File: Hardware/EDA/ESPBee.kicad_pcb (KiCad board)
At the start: 2 copper layers, 24.4 x 27.6 mm, 8 parts, among them P1 HEADER_M_XBEE_P1-P10_PTH_DTE, P2 HEADER_M_XBEE_P11-P20_PTH_DTE, U1 ESP-12E

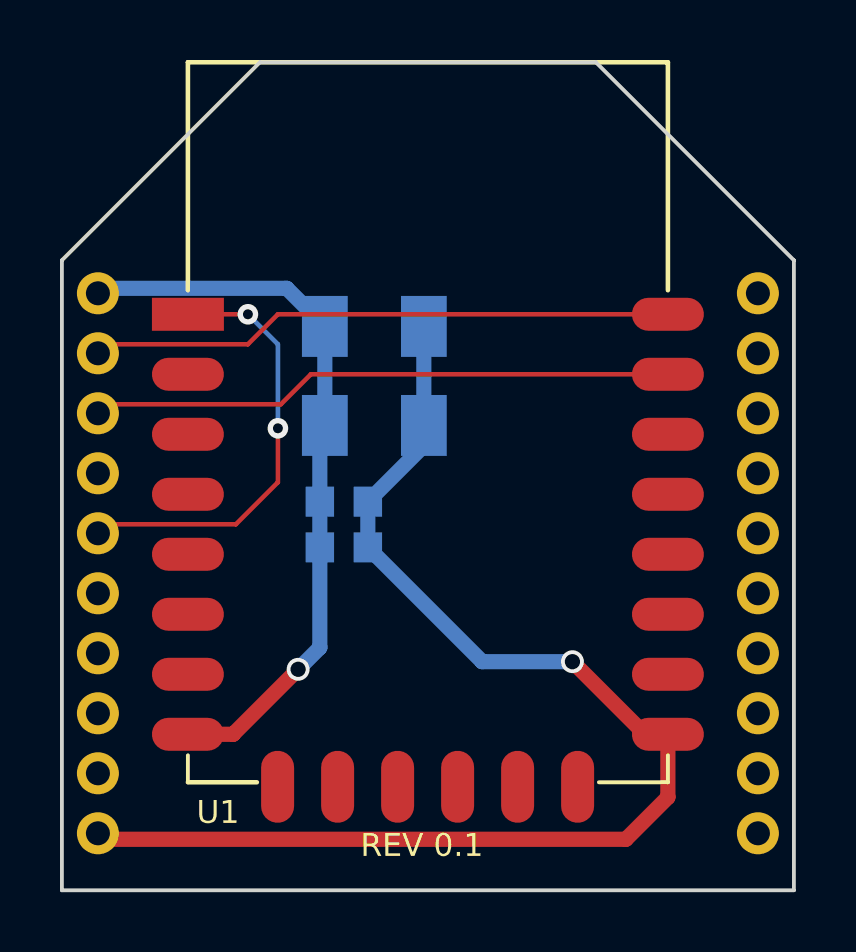
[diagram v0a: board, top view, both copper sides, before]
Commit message: Fixed connections and added pull-up/down resistors for configuration pins.
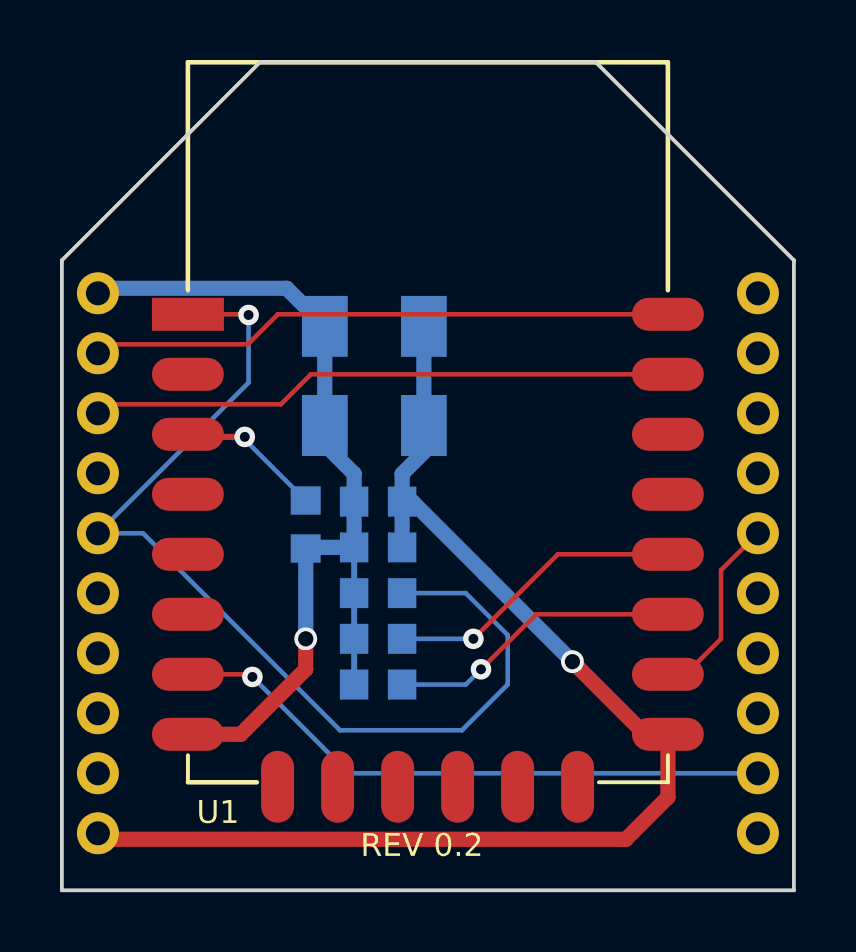
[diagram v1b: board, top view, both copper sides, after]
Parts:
- added R1: 10K, Passive:R0603, B.Cu at (109.5, 95.1)
- added R2: 10K, Passive:R0603, B.Cu at (109.5, 96.6)
- added R3: 10K, Passive:R0603, B.Cu at (107.1, 92.8)
- added R4: 10K, Passive:R0603, B.Cu at (109.5, 98.1)
- G1: value LOGO -> Casco_Logix_Logo
- P1: value HEADER_M_XBEE_P1-P10_PTH_DTE -> XBEE HEADER
- moved C1 1.14 mm to (109.5, 92.0)
- moved C2 1.14 mm to (109.5, 93.6)
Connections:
- U1 pad 16: Net-(U1-Pad16) -> RTS_HEADER
- U1 pad 18: Net-(U1-Pad18) -> /UPLOAD
- U1 pad 7: Net-(U1-Pad7) -> CTS_HEADER
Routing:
- net CTS_HEADER: track 0.00 -> 20.4 mm, vias 0 -> 1
- net RESET: track 14.7 -> 34.1 mm, vias 2 -> 1
- net /UPLOAD: track 0.00 -> 10.0 mm, vias 0 -> 1
- net Net-(R4-Pad2): track 0.00 -> 9.83 mm, vias 0 -> 1
- net VDD: track 24.5 -> 31.2 mm
- net RTS_HEADER: track 0.00 -> 6.29 mm
- net Net-(R3-Pad2): track 0.00 -> 4.89 mm, vias 0 -> 1
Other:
- board text added: "REV 0.2"
- board text removed: "REV 0.1"
